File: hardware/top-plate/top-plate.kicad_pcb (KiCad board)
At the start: 2 copper layers, 77.2 x 77.2 mm, 48 parts

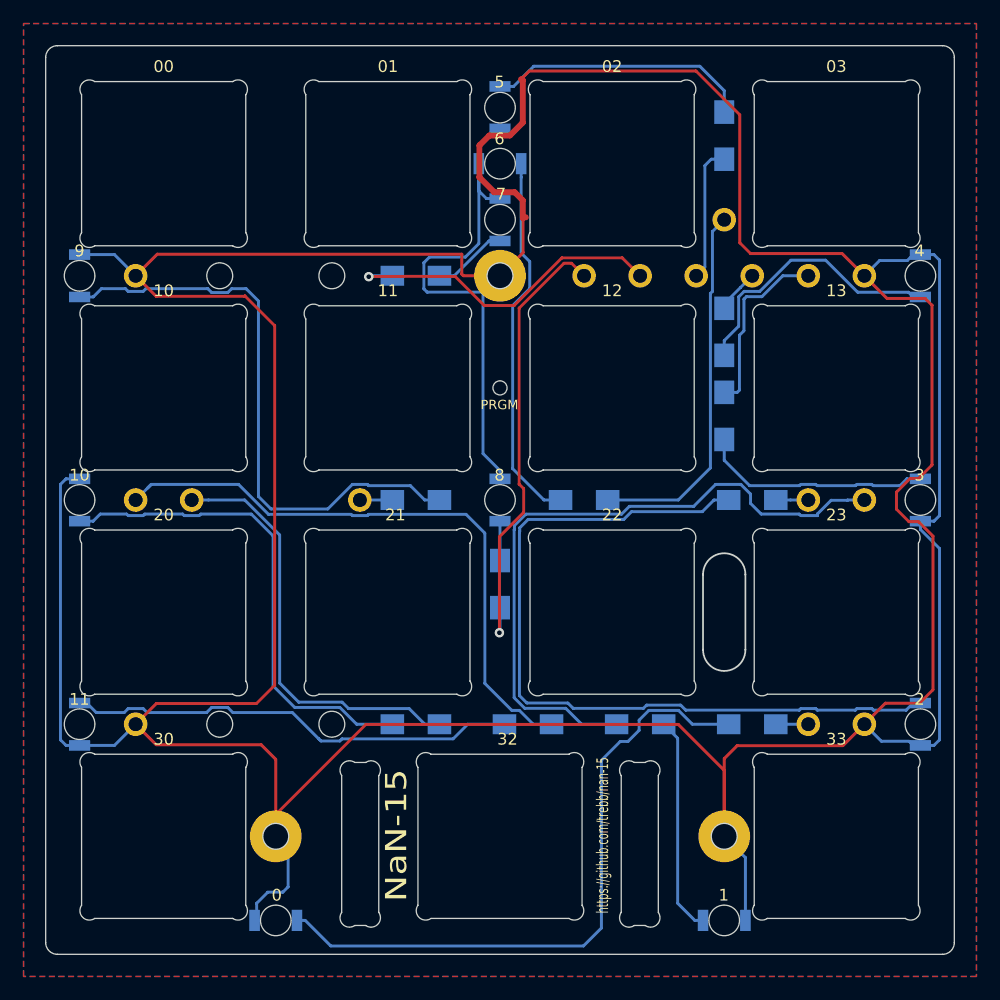
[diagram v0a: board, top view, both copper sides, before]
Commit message: Update version numbers on PCB silkscreens
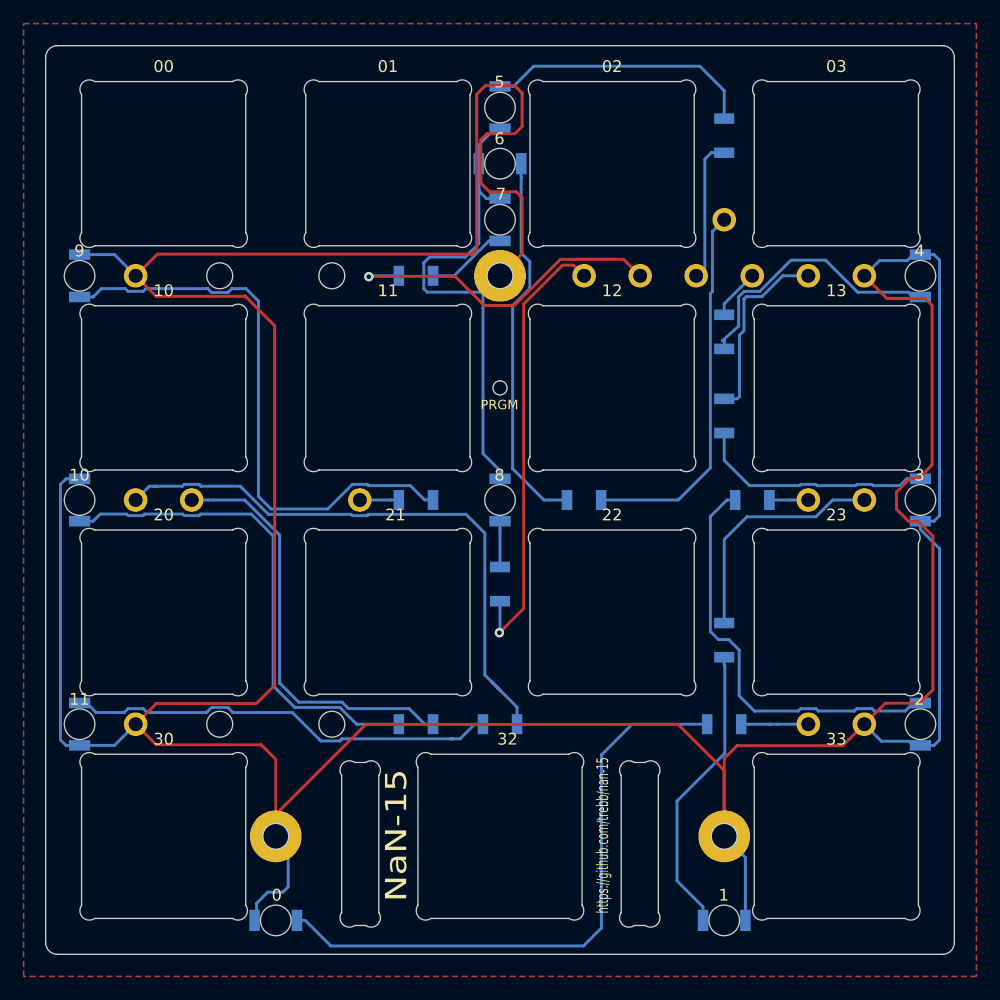
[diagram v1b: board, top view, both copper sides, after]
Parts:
- D0, D1, D10, D3, D6, D8: value Led_Small -> Led_Red
- D11, D2, D4, D5, D7, D9: value Led_Small -> Led_Yellow
- R0, R1, R10, R3, R6, R8: value 480 -> 430; footprint Resistors_SMD:R_1206_HandSoldering -> Resistors_SMD:R_1206
- R11, R2, R4, R5, R7, R9: value 480 -> 560; footprint Resistors_SMD:R_1206_HandSoldering -> Resistors_SMD:R_1206
- moved R1 10.1 mm to (163.7, 102.1), turned to 270 degrees
- moved R0 2.38 mm to (163.7, 109.2)
- moved R11 2.38 mm to (144.7, 109.2)
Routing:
- net /led1: track 57.8 -> 20.4 mm
- net Net-(D2-Pad2): track 68.4 -> 36.0 mm
- net GND: track 456.2 -> 425.9 mm
- net Net-(D1-Pad2): track 18.5 -> 25.0 mm
- net Net-(D0-Pad2): track 55.2 -> 52.2 mm
- net /led0: track 2.76 -> 5.77 mm
- net Net-(D11-Pad2): track 38.7 -> 37.1 mm
- net /led11: track 52.4 -> 50.9 mm
- net Net-(D4-Pad2): track 24.3 -> 23.2 mm
- net Net-(D9-Pad2): track 50.2 -> 49.7 mm
- net Net-(D8-Pad2): track 3.34 -> 3.89 mm
- net Net-(D7-Pad2): track 6.37 -> 6.92 mm
- net Net-(D6-Pad2): track 32.0 -> 32.5 mm
- net Net-(D10-Pad2): track 41.9 -> 42.5 mm
- net /led9: track 2.76 -> 3.31 mm
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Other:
- outline, holes or cut-outs redrawn
- board text added: "v0.2"
- board text removed: "v0.1"
